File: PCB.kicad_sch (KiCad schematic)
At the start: 48 parts, among them U1 WeMos_D1_mini

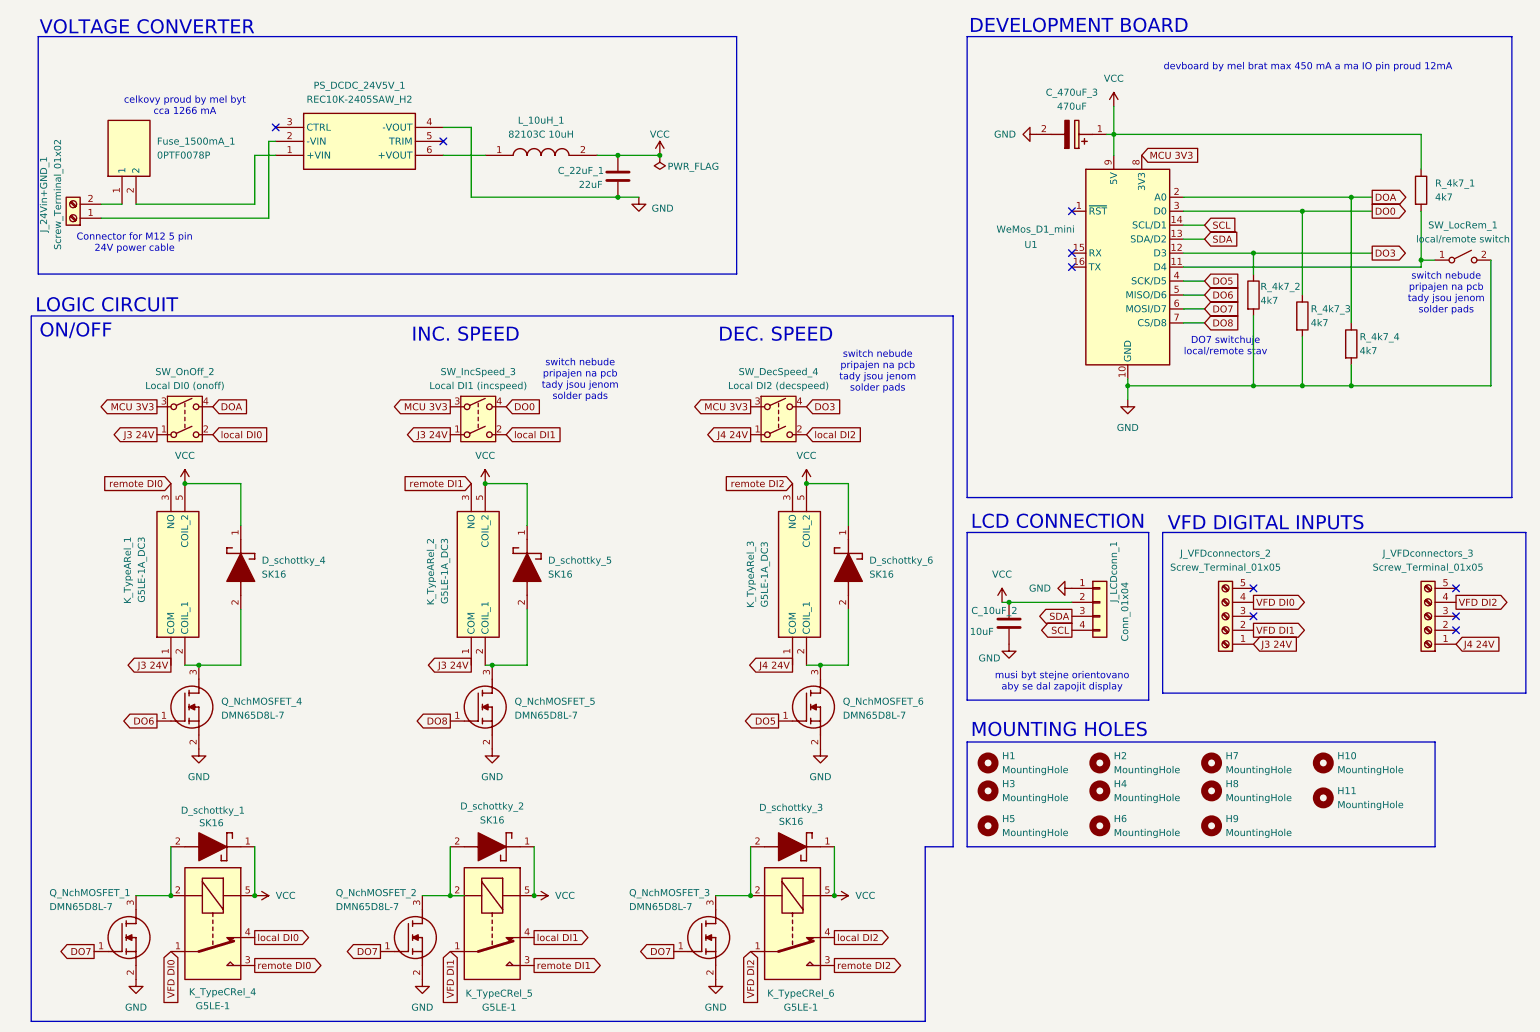
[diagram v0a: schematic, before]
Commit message: Vymena der s reliefem za screw-in connectory
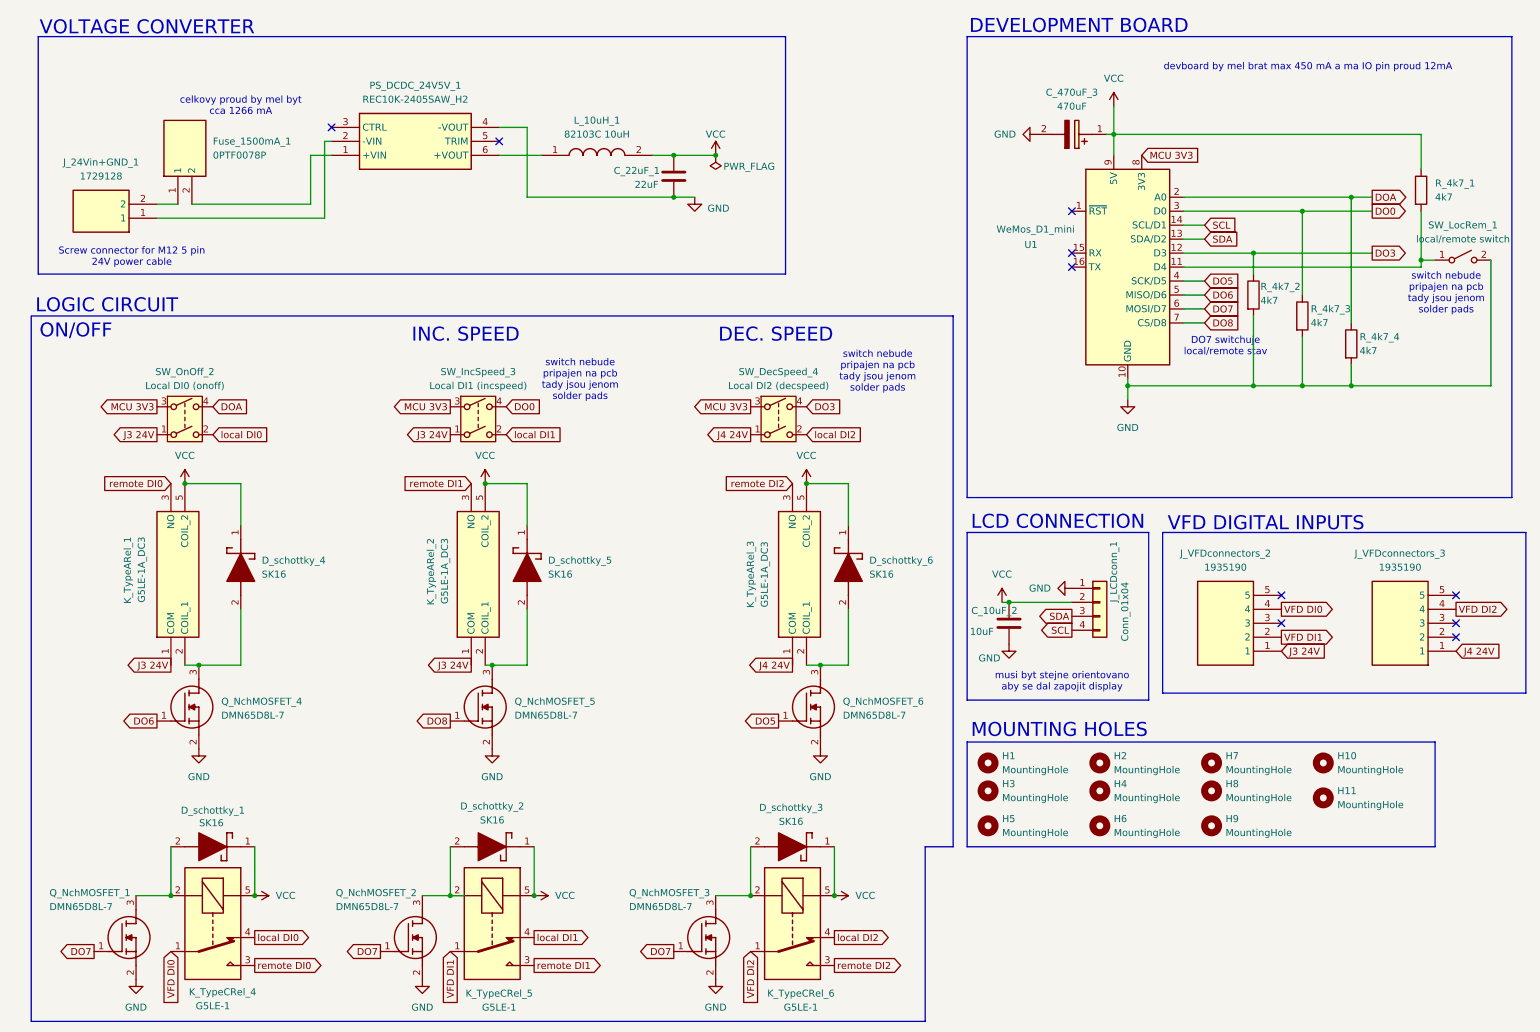
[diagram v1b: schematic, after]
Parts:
- removed J_24Vin+GND_1: Screw_Terminal_01x02, 1x2 screw conn:1729128, symbol Connector:Screw_Terminal_01x02
- removed J_VFDconnectors_2, J_VFDconnectors_3: Screw_Terminal_01x05, 1x5 screw conn:1935190, symbol Connector:Screw_Terminal_01x05
- added J_24Vin+GND_1: 1729128, 1x2 screw conn:1729128, symbol 1x2 screw conn:1729128
- added J_VFDconnectors_2, J_VFDconnectors_3: 1935190, 1x5 screw conn:1935190, symbol 1x5 screw conn:1935190
- SW_LocRem_1: footprint Connector_Wire:SolderWire-0.5sqmm_1x02_P4.8mm_D0.9mm_OD2.3mm_Relief -> 1x2 screw conn:1729128
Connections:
- net J3 24V: now also J_VFDconnectors_2.1
- net J4 24V: now also J_VFDconnectors_3.1
- net VFD DI0: now also J_VFDconnectors_2.4
- net VFD DI1: now also J_VFDconnectors_2.2
- net VFD DI2: now also J_VFDconnectors_3.4
- net at Fuse_1500mA_1.1: now also J_24Vin+GND_1.2
- net at PS_DCDC_24V5V_1.2 (-VIN): now also J_24Vin+GND_1.1
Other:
- note added: "Screw connector for M12 5 pin 24V power cable"
- note removed: "Connector for M12 5 pin 24V power cable"
- moved on the sheet: C_22uF_1, Fuse_1500mA_1, L_10uH_1, PS_DCDC_24V5V_1

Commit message: komponenty jsou rozlozeny spravne a zacinam delat cesty
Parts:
- removed J_24Vin+GND_1: 1729128, 1x2 screw conn:1729128, symbol 1x2 screw conn:1729128
- removed J_VFDconnectors_2, J_VFDconnectors_3: 1935190, 1x5 screw conn:1935190, symbol 1x5 screw conn:1935190
- added J_24Vin+GND_1: Screw_Terminal_01x02, 1x2 screw conn:1729128, symbol Connector:Screw_Terminal_01x02
- added J_VFDconnectors_2, J_VFDconnectors_3: Screw_Terminal_01x05, 1x5 screw conn:1935190, symbol Connector:Screw_Terminal_01x05
- SW_DecSpeed_4, SW_IncSpeed_3, SW_OnOff_2: footprint Connector_Wire:SolderWire-0.5sqmm_1x04_P4.8mm_D0.9mm_OD2.3mm_Relief -> 1x4 screw conn:1935187
- renumbered D_schottky_1 to D_sch_1, D_schottky_2 to D_sch_2, D_schottky_3 to D_sch_3, D_schottky_4 to D_sch_4, D_schottky_5 to D_sch_5, D_schottky_6 to D_sch_6, Q_NchMOSFET_1 to Q_NchFET_1, Q_NchMOSFET_2 to Q_NchFET_2, Q_NchMOSFET_3 to Q_NchFET_3, Q_NchMOSFET_4 to Q_NchFET_4, Q_NchMOSFET_5 to Q_NchFET_5, Q_NchMOSFET_6 to Q_NchFET_6
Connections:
- net J3 24V: now also J_VFDconnectors_2.1 (Pin_1)
- net J4 24V: now also J_VFDconnectors_3.1 (Pin_1)
- net VFD DI0: now also J_VFDconnectors_2.4 (Pin_4)
- net VFD DI1: now also J_VFDconnectors_2.2 (Pin_2)
- net VFD DI2: now also J_VFDconnectors_3.4 (Pin_4)
- net at Fuse_1500mA_1.1: now also J_24Vin+GND_1.2 (Pin_2)
- net at PS_DCDC_24V5V_1.2 (-VIN): now also J_24Vin+GND_1.1 (Pin_1)

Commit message: generovany gerbery z projektu
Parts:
- removed H3, H5, H6, H8: MountingHole, MountingHole:MountingHole_4mm, symbol Mechanical:MountingHole
- removed H4: MountingHole, MountingHole:MountingHole_5mm, symbol Mechanical:MountingHole
- removed H7: MountingHole, MountingHole:MountingHole_3mm, symbol Mechanical:MountingHole
- U_WeMos_D1_Mini_Pro_1: renamed from U1; value WeMos_D1_mini -> WeMos_D1_Mini_Pro
- renumbered H10 to H3, H9 to H4, H11 to H5
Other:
- moved on the sheet: H3, H4, H5
